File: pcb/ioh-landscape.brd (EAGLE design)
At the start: 50.8 x 81.3 mm, 35 parts

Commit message: playing around with layouts
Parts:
- moved R3 72.7 mm to (77.5, 17.8)
- moved U$2 66.3 mm to (2.54, 26.7), turned to 0 degrees
- moved QFRONT 54.9 mm to (49.5, 29.2)
- moved LOGO1 50.6 mm to (19.1, 24.1)
- moved U$1 46.2 mm to (38.1, 11.4)
- moved QBACK 45.5 mm to (43.2, 29.2)
- moved QVIBE 45.5 mm to (30.5, 29.2)
- moved R2 44.5 mm to (54.6, 33.0)
- moved S1 43.2 mm to (67.3, 31.8)
- moved R1 43.2 mm to (57.1, 33.0)
- moved JP1 43.0 mm to (24.1, 24.1)
- moved LED2 42.2 mm to (26.7, 36.8)
- moved JP2 42.2 mm to (52.1, 1.27)
- moved LED3 41.8 mm to (34.3, 36.8)
- moved LED4 41.0 mm to (41.9, 36.8)
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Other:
- board size 50.8 x 81.3 mm -> 78.7 x 39.4 mm

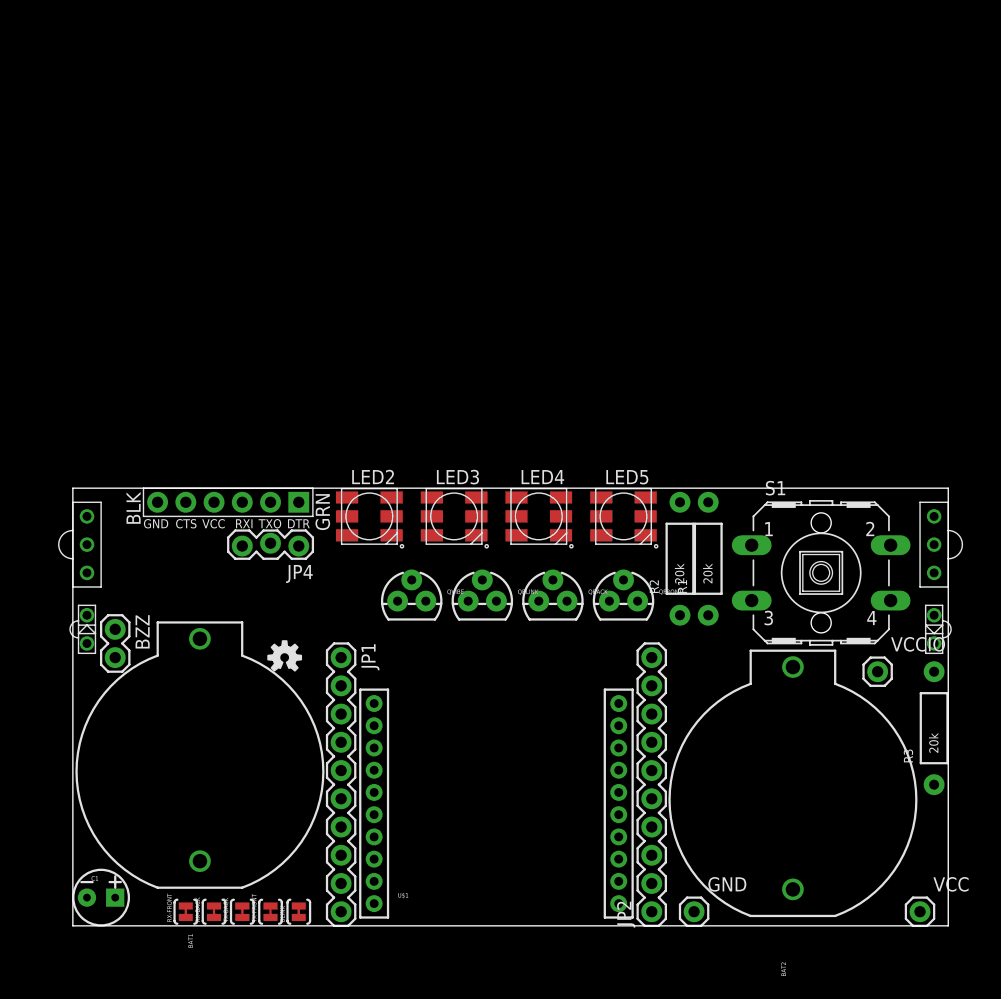
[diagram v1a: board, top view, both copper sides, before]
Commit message: updating due to oshpark drc
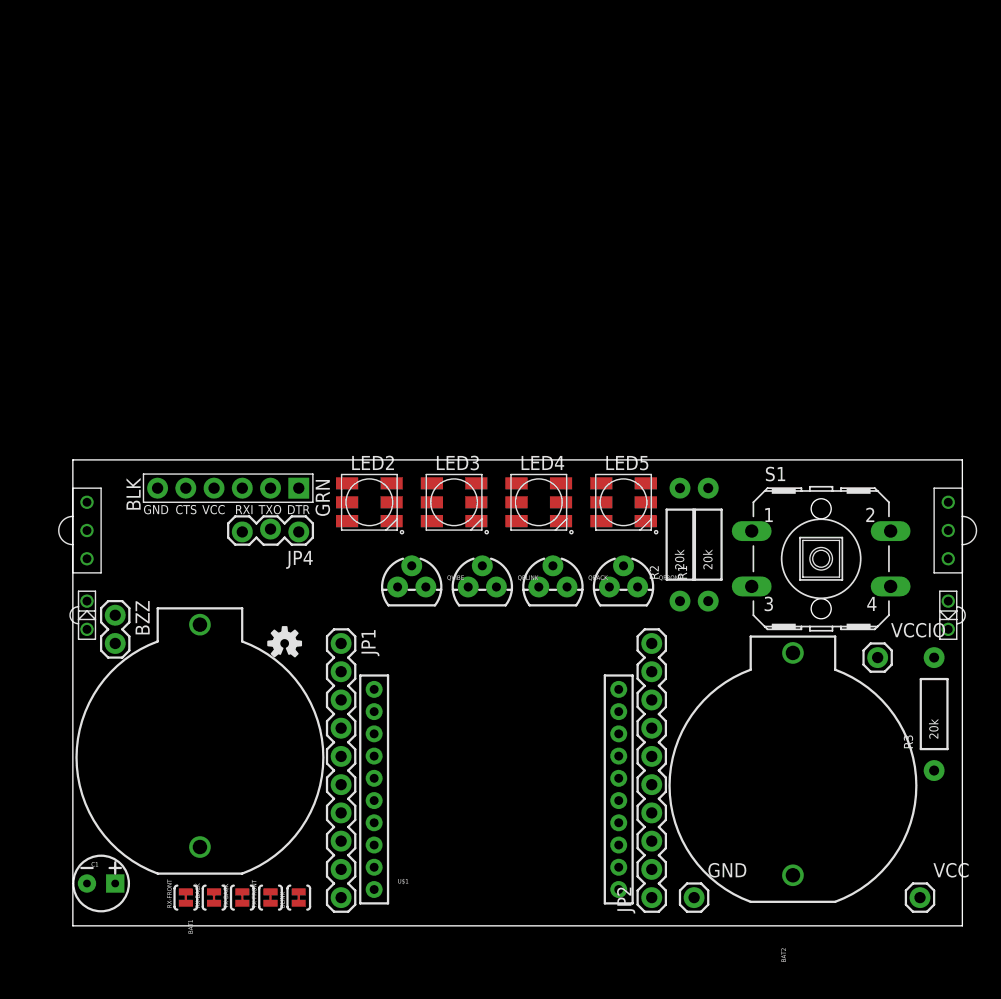
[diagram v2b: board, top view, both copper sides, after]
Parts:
- moved RXBACK 1.80 mm to (78.7, 35.6)
- moved IRBACK 1.80 mm to (78.7, 27.9)
- moved JP4 1.27 mm to (20.3, 35.6)
- moved LED2 1.27 mm to (26.7, 38.1)
- moved LED3 1.27 mm to (34.3, 38.1)
- moved LED4 1.27 mm to (41.9, 38.1)
- moved LED5 1.27 mm to (49.5, 38.1)
- moved RXFRONT 1.27 mm to (1.27, 35.6)
- moved S1 1.27 mm to (67.3, 33.0)
- moved BLINK 1.27 mm to (20.3, 2.54)
- moved C1 1.27 mm to (2.54, 3.81)
- moved GND 1.27 mm to (55.9, 2.54)
- moved JP2 1.27 mm to (52.1, 2.54)
- moved RX-BACK 1.27 mm to (12.7, 2.54)
- moved RX-FRONT 1.27 mm to (10.2, 2.54)
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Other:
- board size 78.7 x 39.4 mm -> 80 x 41.9 mm

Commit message: most power routed
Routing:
- net N$14: track 0.00 -> 128.2 mm, vias 0 -> 5
- net VCC: track 0.00 -> 51.5 mm, vias 0 -> 1
- net VCCIO: track 0.00 -> 22.0 mm, vias 0 -> 3
- net VCCFTDI: track 0.00 -> 4.99 mm
- added copper zone on layer 16, net GND
- added copper zone on layer 16, net N$7

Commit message: autorouted
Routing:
- net N$15: track 0.00 -> 107.1 mm, vias 0 -> 1
- net RXBACK: track 0.00 -> 96.2 mm, vias 0 -> 4
- net TX0: track 0.00 -> 96.1 mm
- net VCCIO: track 22.0 -> 100.6 mm, vias 3 -> 5
- net VCC: track 51.5 -> 127.4 mm
- net TXFRONT: track 0.00 -> 73.7 mm, vias 0 -> 1
- net N$11: track 0.00 -> 68.8 mm, vias 0 -> 1
- net N$4: track 0.00 -> 63.4 mm, vias 0 -> 1
- net N$21: track 0.00 -> 57.6 mm, vias 0 -> 2
- net N$20: track 0.00 -> 53.8 mm, vias 0 -> 2
- net TXBACK: track 0.00 -> 51.6 mm, vias 0 -> 2
- net N$6: track 0.00 -> 48.8 mm, vias 0 -> 3
- net N$17: track 0.00 -> 47.5 mm, vias 0 -> 1
- net VIBE: track 0.00 -> 42.4 mm, vias 0 -> 1
- net BLINK5: track 0.00 -> 42.3 mm, vias 0 -> 1
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
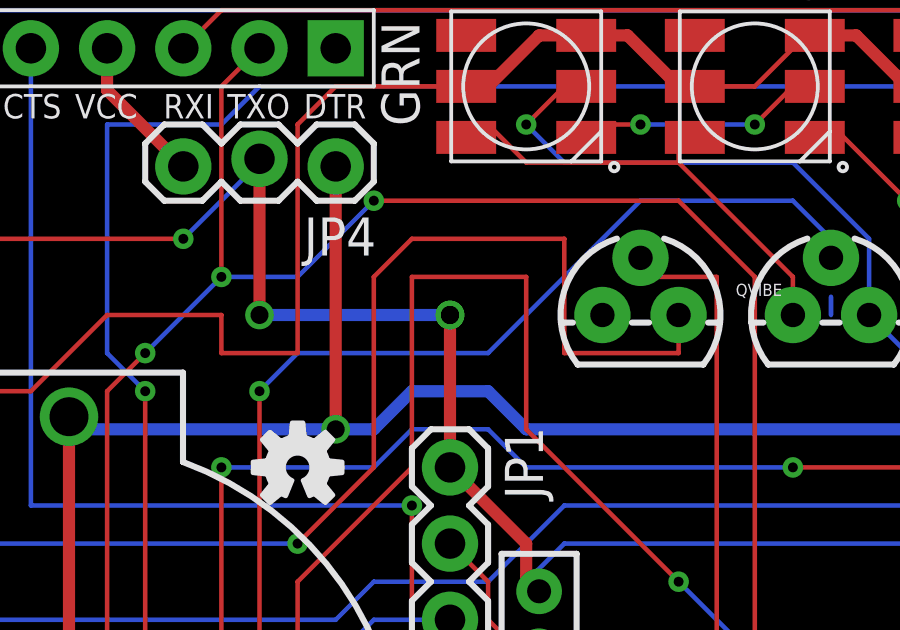
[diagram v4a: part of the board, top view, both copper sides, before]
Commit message: removed via on top of via issue
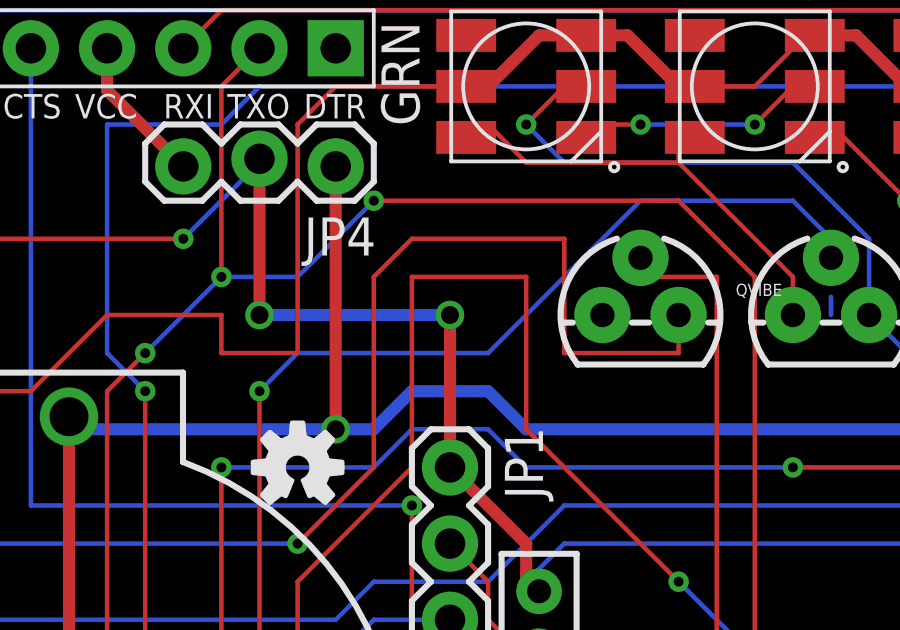
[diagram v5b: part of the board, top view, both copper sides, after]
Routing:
- net VCCIO: vias 5 -> 4
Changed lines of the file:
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@@
 <wire x1="24.13" y1="25.4" x2="24.13" y2="30.48" width="0.4064" layer="1"/>
-<via x="24.13" y="30.48" extent="1-16" drill="0.6" shape="square"/>
 <via x="24.13" y="30.48" extent="1-16" drill="0.6" shape="square"/>
 <wire x1="24.13" y1="30.48" x2="17.78" y2="30.48" width="0.4064" layer="16"/>
